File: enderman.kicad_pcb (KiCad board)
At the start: 2 copper layers, 29 x 98 mm, 23 parts, among them U1 4030, U2 LM556

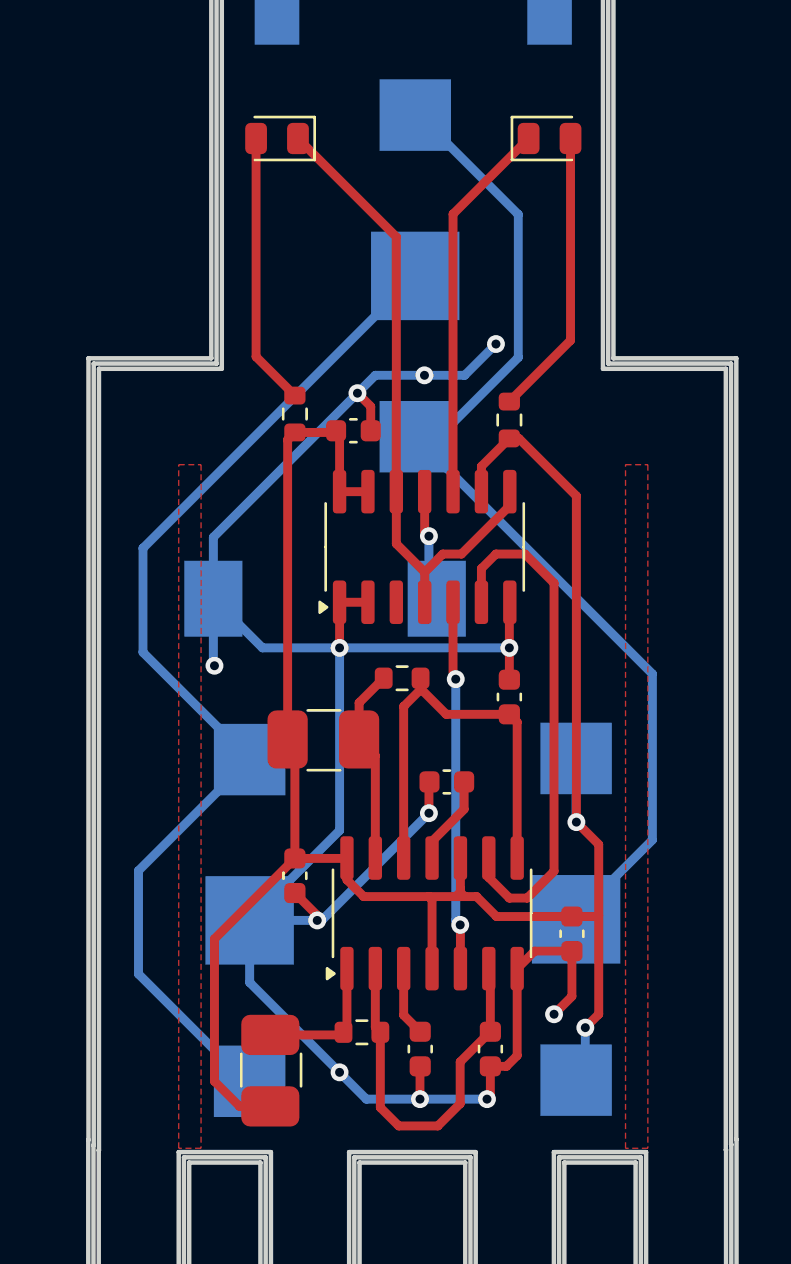
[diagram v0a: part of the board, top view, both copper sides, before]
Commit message: minimize vias
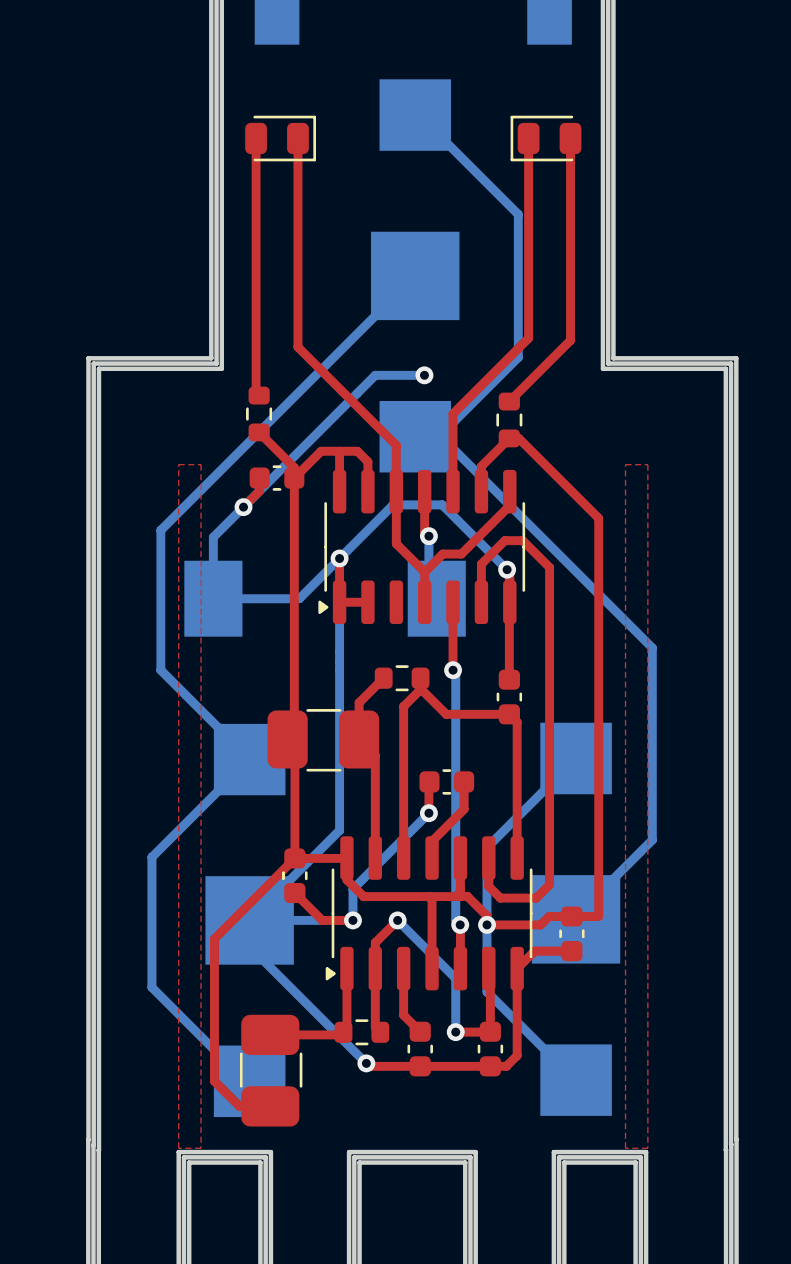
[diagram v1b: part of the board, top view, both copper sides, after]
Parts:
- moved C7 4.02 mm to (132.6, 62.4), turned to 0 degrees
- moved R5 1.60 mm to (131.8, 59.5)
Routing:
- net +6V: track 97.6 -> 106.9 mm, vias 2 -> 1
- net GND: track 101.6 -> 98.1 mm, vias 12 -> 7
- net Net-(U2A-THR): track 17.3 -> 16.0 mm, vias 0 -> 2
- net Net-(U2B-Q): track 23.1 -> 24.3 mm
- net Net-(BT1-+): track 47.3 -> 46.1 mm
- net Net-(BT2--): track 46.3 -> 47.0 mm
- net Net-(D1-A): track 12.2 -> 11.6 mm
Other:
- board text added: "REYWAS INDUSTRIES 2025"
- board text removed: "REYWAS INDSTRIES 2025"

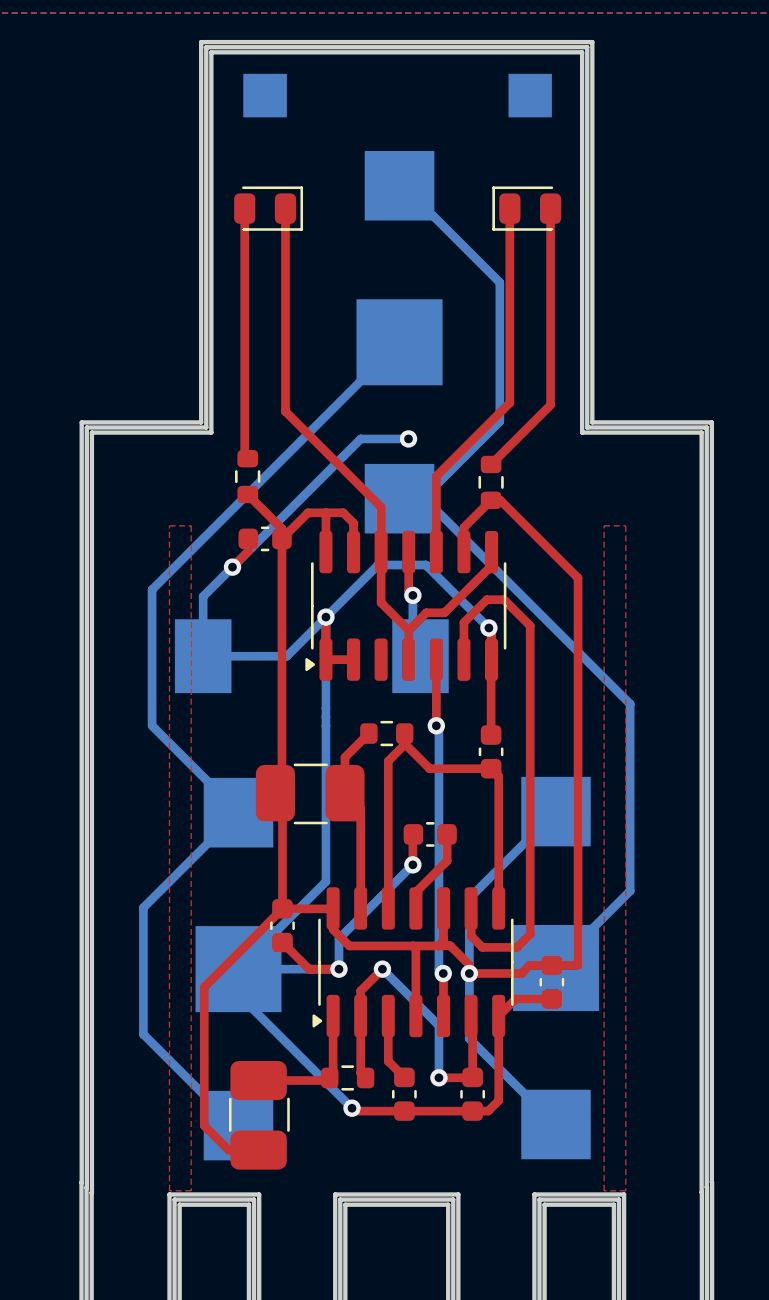
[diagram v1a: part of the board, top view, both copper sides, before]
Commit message: routed atari punk console version
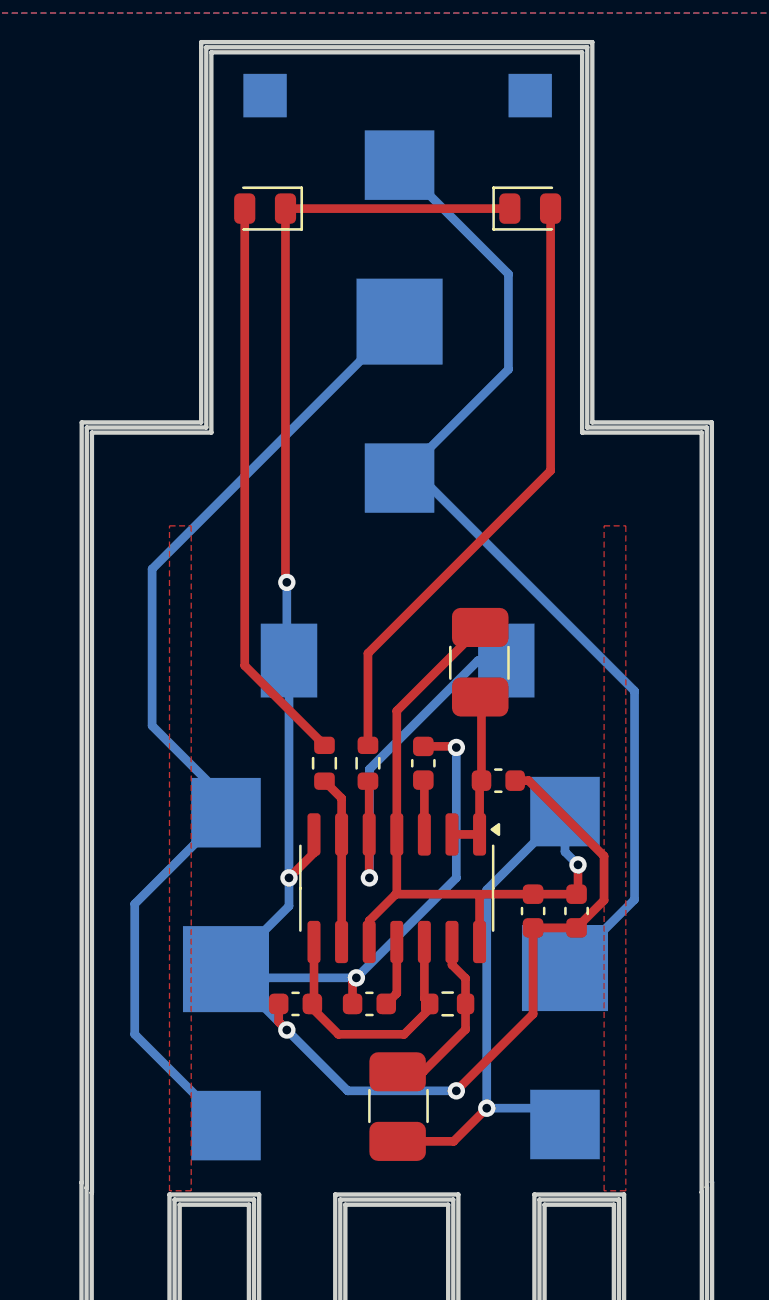
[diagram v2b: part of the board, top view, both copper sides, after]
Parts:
- removed C7: 100n, Capacitor_SMD:C_0603_1608Metric
- removed R4: 10k, Resistor_SMD:R_0603_1608Metric
- removed U2: LM556, Package_SO:SOIC-14_3.9x8.7mm_P1.27mm
- U1: value 4030 -> LM556
- moved R3 23.4 mm to (142.6, 68.0), turned to -90 degrees
- moved C4 15.3 mm to (139.9, 72.7), turned to 90 degrees
- moved R2 15.1 mm to (138.6, 88.6), turned to 90 degrees
- moved C2 14.7 mm to (134.0, 83.8), turned to 180 degrees
- moved C5 14.5 mm to (143.3, 73.5), turned to 0 degrees
- moved R6 14.1 mm to (137.3, 72.7), turned to 90 degrees
- moved R5 13.7 mm to (135.3, 72.7), turned to 90 degrees
- moved U1 13.0 mm to (138.7, 78.5), turned to -90 degrees
- moved R1 12.8 mm to (141.0, 83.8), turned to 180 degrees
- moved C6 11.6 mm to (144.9, 79.5)
- moved C3 8.29 mm to (137.4, 83.8)
- moved LS1 3.96 mm to (139.4, 68.4)
- moved C1 3.47 mm to (146.9, 79.5)
- moved BT3 0.95 mm to (132.3, 51.9)
- moved BT1 0.57 mm to (137.3, 82.8)
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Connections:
- C2 pad 1: Net-(U2B-THR) -> Net-(U1B-THR)
- C3 pad 1: Net-(U2B-CV) -> Net-(U1B-CV)
- C4 pad 1: Net-(U2A-CV) -> Net-(U1A-CV)
- C5 pad 1: Net-(U2A-THR) -> Net-(U1A-DIS)
- D1 pad 1: Net-(D1-K) -> GND
- D2 pad 1: Net-(D2-K) -> GND
- LS1 pad 1: Net-(LS1-Pad1) -> Net-(U1A-Q)
- R1 pad 1: Net-(U2B-DIS) -> Net-(U1B-DIS)
- R1 pad 2: Net-(U2B-THR) -> Net-(U1B-THR)
- R2 pad 2: Net-(U2B-DIS) -> Net-(U1B-DIS)
- R3 pad 2: Net-(U2A-DIS) -> Net-(U1A-DIS)
- R5 pad 1: Net-(D1-A) -> Net-(U1A-TR)
- R5 pad 2: +6V -> Net-(D1-A)
- R6 pad 1: Net-(D2-A) -> Net-(U1A-Q)
- R6 pad 2: +6V -> Net-(D2-A)
- U1 pad 1: GND -> Net-(U1A-DIS)
- U1 pad 10: Net-(D2-K) -> +6V
- U1 pad 11: Net-(LS1-Pad1) -> Net-(U1B-CV)
- U1 pad 12: Net-(D1-K) -> Net-(U1B-THR)
- U1 pad 13: +6V -> Net-(U1B-DIS)
- U1 pad 2: GND -> Net-(U1A-DIS)
- U1 pad 3: unconnected-(U1-Pad3) -> Net-(U1A-CV)
- U1 pad 4: Net-(D1-K) -> +6V
- U1 pad 5: Net-(U2A-Q) -> Net-(U1A-Q)
- U1 pad 6: Net-(U2B-Q) -> Net-(U1A-TR)
- U1 pad 8: Net-(D1-K) -> Net-(U1B-THR)
- U1 pad 9: +6V -> Net-(U1A-TR)
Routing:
- net +6V: track 106.9 -> 55.0 mm, vias 1 -> 2
- net Net-(D1-K): track 28.8 -> 0.00 mm
- net Net-(U2B-Q): track 24.3 -> 0.00 mm
- net Net-(U2B-THR): track 19.9 -> 0.00 mm
- net Net-(U1A-Q): track 0.00 -> 17.8 mm, vias 0 -> 1
- net Net-(D2-K): track 17.2 -> 0.00 mm
- net Net-(U2A-Q): track 16.5 -> 0.00 mm, vias 2 -> 0
- net Net-(U2A-THR): track 16.0 -> 0.00 mm, vias 2 -> 0
- net Net-(D2-A): track 12.9 -> 28.2 mm
- net Net-(D1-A): track 11.6 -> 26.2 mm
- net Net-(U1B-THR): track 0.00 -> 12.6 mm
- net Net-(U2B-DIS): track 8.81 -> 0.00 mm
- net Net-(U1B-DIS): track 0.00 -> 8.22 mm
- net Net-(U1A-TR): track 0.00 -> 7.73 mm
- net Net-(U1A-DIS): track 0.00 -> 7.66 mm
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
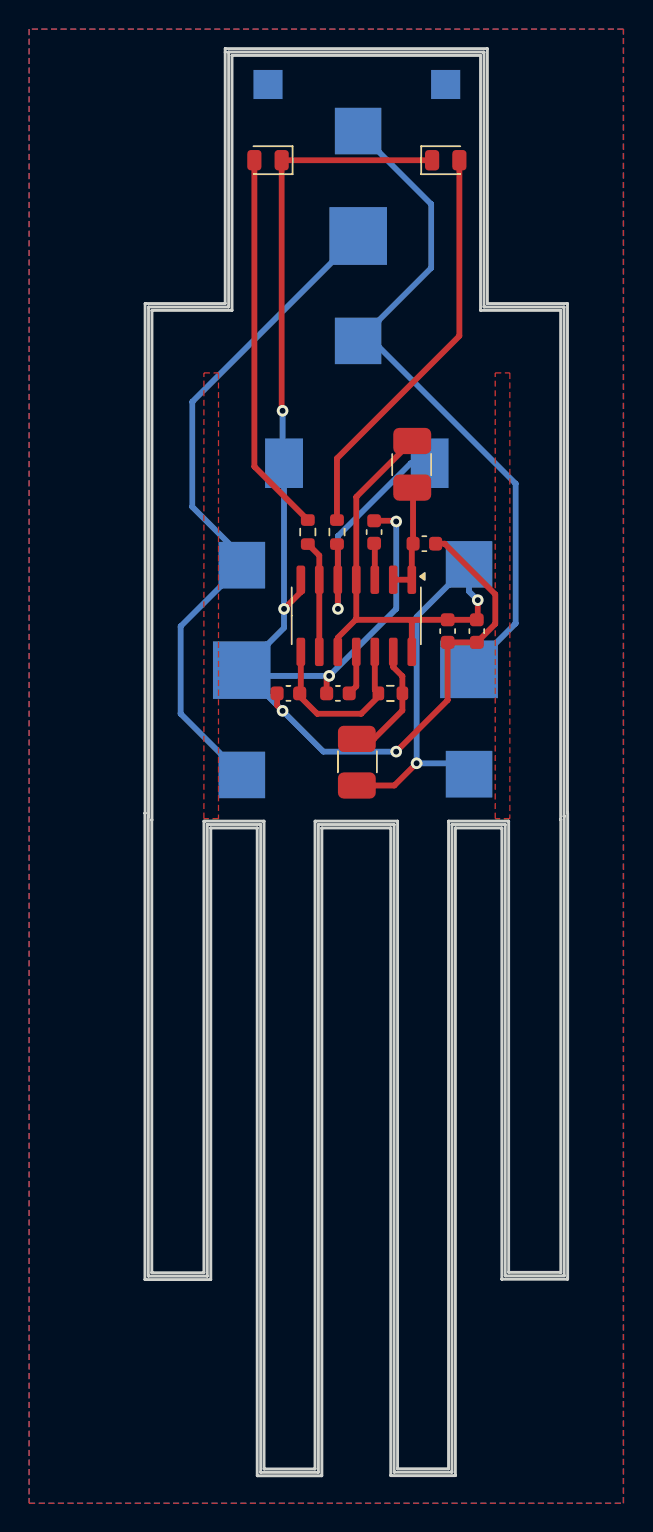
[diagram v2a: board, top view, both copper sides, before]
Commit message: updated piezo footprint.  Better routing.  Added on/off switch.  Hid some vias under chip.
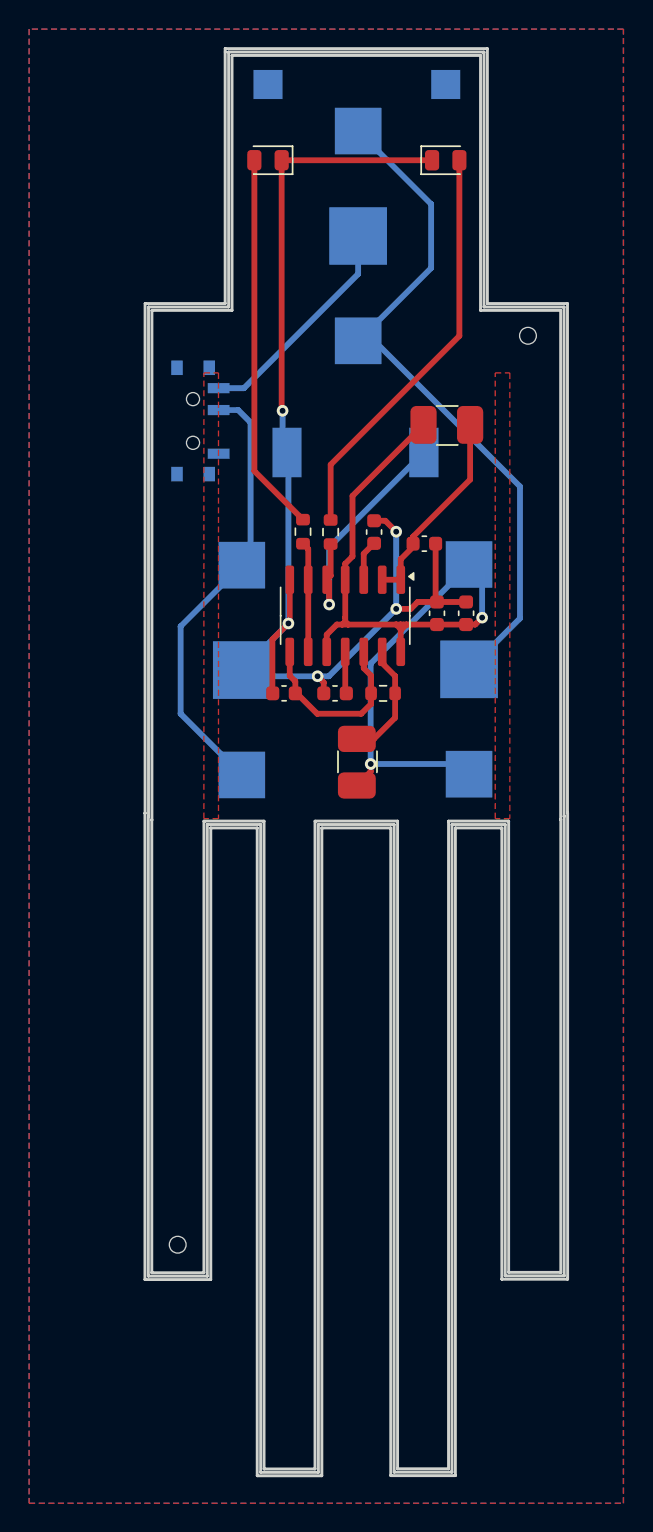
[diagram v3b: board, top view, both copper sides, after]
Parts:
- added SW1: SW_SPDT, Button_Switch_SMD:SW_SPDT_PCM12, B.Cu at (127.8, 65.1)
- moved R3 3.51 mm to (144.8, 65.3), turned to 0 degrees
- moved LS1 1.43 mm to (138.6, 67.2)
- moved C1 1.43 mm to (146.2, 78.3), turned to 90 degrees
- moved C6 1.43 mm to (144.2, 78.3), turned to -90 degrees
- moved U1 0.76 mm to (137.9, 78.5)
- moved R1 0.50 mm to (140.5, 83.8)
- moved R6 0.43 mm to (136.9, 72.7)
- moved R5 0.33 mm to (135.0, 72.7)
- moved C2 0.30 mm to (133.7, 83.8)
- moved C3 0.20 mm to (137.2, 83.8)
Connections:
- BT3 pad 2: Net-(BT1-+) -> Net-(BT3--)
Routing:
- net GND: track 105.1 -> 85.4 mm, vias 6 -> 5
- net Net-(BT1-+): track 46.8 -> 30.5 mm
- net Net-(BT3--): track 0.00 -> 15.4 mm
- net Net-(U1A-DIS): track 7.66 -> 13.9 mm
- net +6V: track 55.0 -> 60.5 mm
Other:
- outline, holes or cut-outs redrawn

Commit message: atari punk version
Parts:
- moved D2 0.40 mm to (144.4, 47.2)
- moved SW1 0.22 mm to (128.0, 65.1)
- moved D1 0.20 mm to (132.8, 47.2)
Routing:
- net GND: track 85.4 -> 84.8 mm
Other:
- board size 29 x 98 mm -> 28 x 97 mm
